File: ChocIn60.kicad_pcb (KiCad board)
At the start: 2 copper layers, 100 x 65 mm, 31 parts, among them J1 USB_B_Micro, J2 AVR-ISP-6, J3 Conn_01x30, J4 Conn_01x04, SW1 SW_Push, U1 ATmega32U4-AU, Y1 16MHz

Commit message: 差動ペア配線
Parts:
- D2: footprint Package_TO_SOT_SMD:SOT-143 -> Orbit_locallib:SOT143B
- moved U1 88.7 mm to (88.1, 78.0), turned to 270 degrees
- moved D2 82.8 mm to (57.7, 58.2), turned to 270 degrees
- moved R2 74.8 mm to (56.3, 65.0), turned to 90 degrees
- moved R1 73.0 mm to (59.1, 65.0), turned to 90 degrees
- moved J1 71.3 mm to (58.0, 52.6)
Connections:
- net Net-(D2-Pad2) renamed /D_P
- net Net-(D2-Pad3) renamed /D_N
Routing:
- net D+: track 0.00 -> 34.2 mm
- net D-: track 0.00 -> 34.1 mm
- net /D_P: track 0.00 -> 10.9 mm
- net /D_N: track 0.00 -> 10.9 mm
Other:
- net class V added: clearance 0.2, trace_width 0.4, via_dia 0.8, via_drill 0.4

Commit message: [WIP] 電源周り
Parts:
- moved D1 91.2 mm to (49.5, 83.8), turned to 90 degrees
- moved F1 82.9 mm to (49.5, 75.8), turned to 90 degrees
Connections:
- U1 pad 14: GND -> +5V
- U1 pad 24: GND -> +5V
- U1 pad 34: GND -> +5V
- U1 pad 44: GND -> +5V
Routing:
- net VCC: track 0.00 -> 23.2 mm
- net VBUS: track 0.00 -> 4.90 mm
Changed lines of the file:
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@@
     (thickness 1.6)
     (drawings 229)
-    (tracks 30)
+    (tracks 34)
     (zones 0)
     (modules 31)
@@
     (solder_mask_min_width 0.25)
     (aux_axis_origin 0 0)
-    (visible_elements 7FFFF7FF)
+    (visible_elements 7FFFFFFF)
     (pcbplotparams
       (layerselection 0x010fc_ffffffff)
@@
     )
     (pad 44 smd rect (at -4 5.7 180) (size 1.5 0.55) (layers B.Cu B.Paste B.Mask)
-      (net 1 GND))
+      (net 5 +5V))
     (pad 43 smd rect (at -3.2 5.7 180) (size 1.5 0.55) (layers B.Cu B.Paste B.Mask)
       (net 1 GND))
@@
       (net 1 GND))
     (pad 34 smd rect (at 4 5.7 180) (size 1.5 0.55) (layers B.Cu B.Paste B.Mask)
-      (net 1 GND))
+      (net 5 +5V))
     (pad 33 smd rect (at 5.7 4 270) (size 1.5 0.55) (layers B.Cu B.Paste B.Mask)
       (net 37 "Net-(R5-Pad2)"))
@@
       (net 23 PD4))
     (pad 24 smd rect (at 5.7 -3.2 270) (size 1.5 0.55) (layers B.Cu B.Paste B.Mask)
-      (net 1 GND))
+      (net 5 +5V))
     (pad 23 smd rect (at 5.7 -4 270) (size 1.5 0.55) (layers B.Cu B.Paste B.Mask)
       (net 1 GND))
@@
       (net 1 GND))
     (pad 14 smd rect (at -2.4 -5.7 180) (size 1.5 0.55) (layers B.Cu B.Paste B.Mask)
-      (net 1 GND))
+      (net 5 +5V))
     (pad 13 smd rect (at -3.2 -5.7 180) (size 1.5 0.55) (layers B.Cu B.Paste B.Mask)
       (net 9 ~RESET))
@@
   )
   (module Fuse:Fuse_1206_3216Metric_Pad1.42x1.75mm_HandSolder (layer B.Cu)
-    (at -9.602 17.749)
+    (at 49.53 75.7825 90)
     (descr "Fuse SMD 1206 (3216 Metric), square (rectangular) end terminal, IPC_7351 nominal with elongated pad for handsoldering. (Body size source: http://www.tortai-tech.com/upload/download/2011102023233369053.pdf), generated with kicad-footprint-generator")
     (tags "resistor handsolder")
     (attr smd)
-    (fp_text reference F1 (at 0 1.82) (layer B.SilkS)
-      (effects (font (size 1 1) (thickness 0.15)) (justify mirror))
-    )
-    (fp_text value 500mA (at 0 -1.82) (layer B.Fab)
-      (effects (font (size 1 1) (thickness 0.15)) (justify mirror))
-    )
-    (fp_text user %R (at 0 0) (layer B.Fab)
+    (fp_text reference F1 (at 0 1.82 90) (layer B.SilkS)
+      (effects (font (size 1 1) (thickness 0.15)) (justify mirror))
+    )
+    (fp_text value 500mA (at 0 -1.82 90) (layer B.Fab)
+      (effects (font (size 1 1) (thickness 0.15)) (justify mirror))
+    )
+    (fp_text user %R (at 0 0 90) (layer B.Fab)
       (effects (font (size 0.8 0.8) (thickness 0.12)) (justify mirror))
     )
@@
     (fp_line (start -1.6 0.8) (end 1.6 0.8) (layer B.Fab) (width 0.1))
     (fp_line (start -1.6 -0.8) (end -1.6 0.8) (layer B.Fab) (width 0.1))
-    (pad 2 smd roundrect (at 1.4875 0) (size 1.425 1.75) (layers B.Cu B.Paste B.Mask) (roundrect_rratio 0.175439)
+    (pad 2 smd roundrect (at 1.4875 0 90) (size 1.425 1.75) (layers B.Cu B.Paste B.Mask) (roundrect_rratio 0.175439)
       (net 7 VCC))
-    (pad 1 smd roundrect (at -1.4875 0) (size 1.425 1.75) (layers B.Cu B.Paste B.Mask) (roundrect_rratio 0.175439)
+    (pad 1 smd roundrect (at -1.4875 0 90) (size 1.425 1.75) (layers B.Cu B.Paste B.Mask) (roundrect_rratio 0.175439)
       (net 6 VBUS))
     (model ${KISYS3DMOD}/Fuse.3dshapes/Fuse_1206_3216Metric.wrl
@@
   )
   (module Diode_SMD:D_SOD-123 (layer B.Cu)
-    (at -9.702 14.429)
+    (at 49.53 83.82 90)
     (descr SOD-123)
     (tags SOD-123)
     (attr smd)
-    (fp_text reference D1 (at 0 2) (layer B.SilkS)
-      (effects (font (size 1 1) (thickness 0.15)) (justify mirror))
-    )
-    (fp_text value Schottky (at 0 -2.1) (layer B.Fab)
+    (fp_text reference D1 (at 0 2 90) (layer B.SilkS)
+      (effects (font (size 1 1) (thickness 0.15)) (justify mirror))
+    )
+    (fp_text value Schottky (at 0 -2.1 90) (layer B.Fab)
       (effects (font (size 1 1) (thickness 0.15)) (justify mirror))
     )
@@
     (fp_line (start 0.25 0) (end 0.75 0) (layer B.Fab) (width 0.1))
     (fp_line (start -2.25 1) (end -2.25 -1) (layer B.SilkS) (width 0.12))
-    (fp_text user %R (at 0 2) (layer B.Fab)
-      (effects (font (size 1 1) (thickness 0.15)) (justify mirror))
-    )
-    (pad 2 smd rect (at 1.65 0) (size 0.9 1.2) (layers B.Cu B.Paste B.Mask)
+    (fp_text user %R (at 0 2 90) (layer B.Fab)
+      (effects (font (size 1 1) (thickness 0.15)) (justify mirror))
+    )
+    (pad 2 smd rect (at 1.65 0 90) (size 0.9 1.2) (layers B.Cu B.Paste B.Mask)
       (net 6 VBUS))
-    (pad 1 smd rect (at -1.65 0) (size 0.9 1.2) (layers B.Cu B.Paste B.Mask)
+    (pad 1 smd rect (at -1.65 0 90) (size 0.9 1.2) (layers B.Cu B.Paste B.Mask)
       (net 5 +5V))
     (model ${KISYS3DMOD}/Diode_SMD.3dshapes/D_SOD-123.wrl
@@
   (gr_line (start 30 86.2) (end 334 86.2) (angle 90) (layer Eco1.User) (width 0.381))
   (gr_line (start 334 107.5) (end 30 107.5) (angle 90) (layer Eco1.User) (width 0.381))
+  (segment (start 49.53 77.27) (end 49.53 82.17) (width 0.4) (layer B.Cu) (net 6))
+  (segment (start 56.7 54.55) (end 56.7 54.05) (width 0.4) (layer B.Cu) (net 7))
+  (segment (start 49.53 61.72) (end 56.7 54.55) (width 0.4) (layer B.Cu) (net 7))
+  (segment (start 49.53 74.295) (end 49.53 61.72) (width 0.4) (layer B.Cu) (net 7))
   (segment (start 57.785 66.421) (end 58.42 65.786) (width 0.2) (layer B.Cu) (net 35))
   (segment (start 57.785 66.929) (end 57.785 66.421) (width 0.2) (layer B.Cu) (net 35))

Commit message: [WIP] 仮配置・仮配線
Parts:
- moved J3 143.3 mm to (110.0, 110.0), turned to 90 degrees
- moved R7 127.7 mm to (111.5, 63.5)
- moved C6 125.2 mm to (90.4, 89.3)
- moved C2 119.6 mm to (98.7, 74.9), turned to 270 degrees
- moved C5 119.3 mm to (79.4, 82.9), turned to 90 degrees
- moved Y1 117.5 mm to (102.6, 77.5), turned to 90 degrees
- moved C3 113.9 mm to (87.2, 65.5), turned to 180 degrees
- moved J2 111.7 mm to (99.0, 63.0), turned to 90 degrees
- moved C4 105.0 mm to (98.6, 70.5), turned to 180 degrees
- moved C1 103.6 mm to (98.7, 78.7), turned to 270 degrees
- moved R5 103.6 mm to (84.1, 90.3), turned to 90 degrees
- moved SW1 99.5 mm to (69.2, 98.2)
- moved C7 99.1 mm to (79.4, 73.2), turned to 90 degrees
- moved J4 95.2 mm to (113.0, 60.5), turned to 90 degrees
- moved R6 93.6 mm to (106.9, 63.5)
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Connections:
- net Net-(C3-Pad1) renamed /UCAP
- C2 pad 1: Net-(C2-Pad1) -> GND
- C2 pad 2: GND -> Net-(C2-Pad2)
- J4 pad 1: +5V -> GND
- J4 pad 2: PD0_SCL -> PD1_SDA
- J4 pad 3: PD1_SDA -> PD0_SCL
- J4 pad 4: GND -> +5V
- R7 pad 1: +5V -> PD1_SDA
- R7 pad 2: PD1_SDA -> +5V
- SW1 pad 1: GND -> ~RESET
- SW1 pad 2: ~RESET -> GND
- SW1 pad 3: GND -> ~RESET
- SW1 pad 4: ~RESET -> GND
- U1 pad 16: Net-(C2-Pad1) -> Net-(C2-Pad2)
- Y1 pad 3: Net-(C2-Pad1) -> Net-(C2-Pad2)
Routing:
- net +5V: track 0.00 -> 117.8 mm, vias 0 -> 6
- net GND: track 0.00 -> 48.6 mm, vias 0 -> 2
- net VBUS: track 4.90 -> 51.7 mm, vias 0 -> 2
- net PD1_SDA: track 0.00 -> 39.7 mm
- net PD0_SCL: track 0.00 -> 38.1 mm
- net PB2_MOSI: track 0.00 -> 14.9 mm
- net ~RESET: track 0.00 -> 13.4 mm, vias 0 -> 1
- net PB3_MISO: track 0.00 -> 12.1 mm
- net Net-(C2-Pad2): track 0.00 -> 11.9 mm
- net PB1_SCK: track 0.00 -> 11.7 mm
- net Net-(C1-Pad1): track 0.00 -> 7.84 mm
- net /UCAP: track 0.00 -> 6.75 mm
- net PB7: track 0.00 -> 4.36 mm, vias 0 -> 1
- net PD2: track 0.00 -> 3.42 mm
- net PD3: track 0.00 -> 2.43 mm
- added copper zone on B.Cu, net GND
- added copper zone on F.Cu, net GND

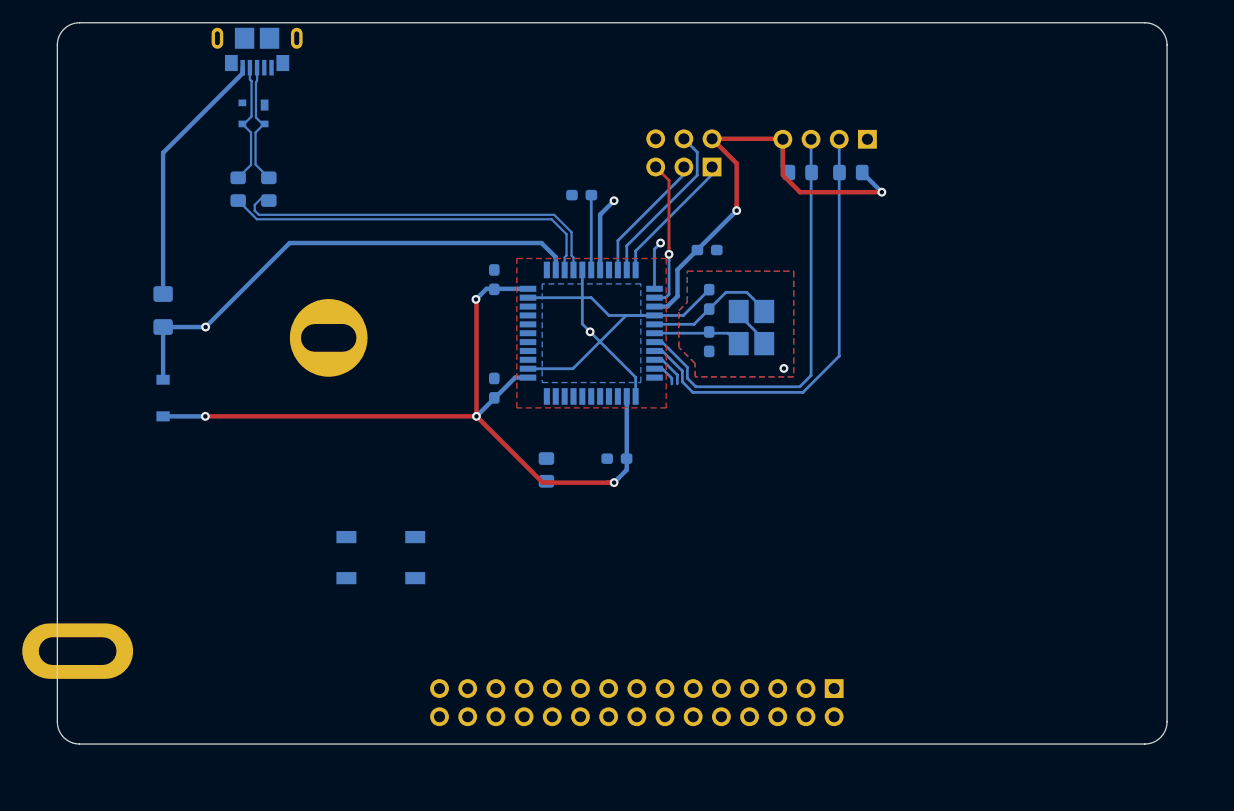
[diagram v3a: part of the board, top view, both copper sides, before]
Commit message: USB-C 復活
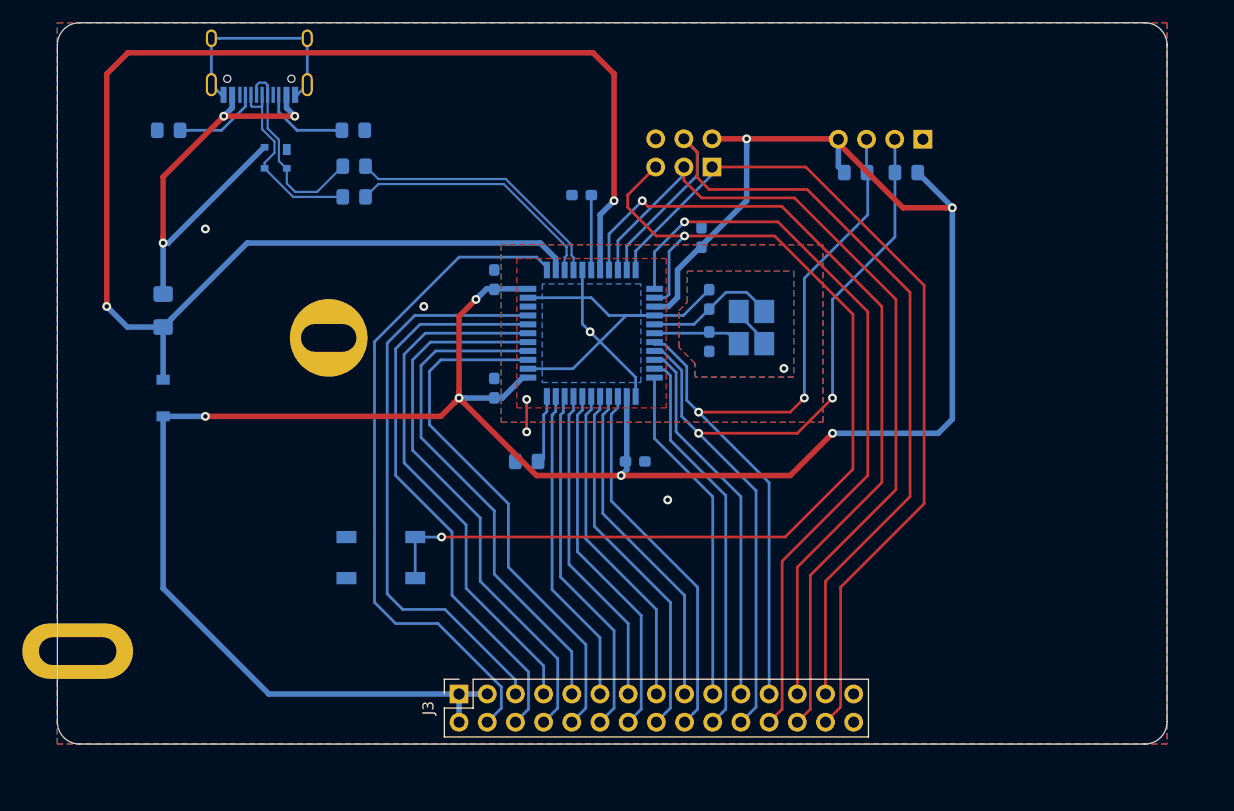
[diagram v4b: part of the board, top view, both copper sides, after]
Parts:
- removed J1: USB_B_Micro, Connector_USB:USB_Micro-B_GCT_USB3076-30-A
- added R3: 5.1k, Resistor_SMD:R_0805_2012Metric_Pad1.15x1.40mm_HandSolder, B.Cu at (66.7, 59.7)
- added R4: 5.1k, Resistor_SMD:R_0805_2012Metric_Pad1.15x1.40mm_HandSolder, B.Cu at (50.0, 59.7)
- added USB1: HRO-TYPE-C-31-M-12, Orbit_Type-C:HRO-TYPE-C-31-M-12, B.Cu at (58.2, 48.8)
- J3: moved to F.Cu
- moved J3 33.8 mm to (76.2, 110.5)
- moved R2 10.5 mm to (66.7, 65.7), turned to 180 degrees
- moved R1 7.96 mm to (66.7, 62.9), turned to 180 degrees
- moved J4 5.00 mm to (118.0, 60.5)
- moved R6 5.00 mm to (111.9, 63.5)
- moved R7 5.00 mm to (116.5, 63.5)
- moved D2 4.47 mm to (59.7, 62.2)
- moved R5 1.93 mm to (82.3, 89.5), turned to 0 degrees
- moved C6 1.67 mm to (92.1, 89.5)
- moved C4 1.24 mm to (98.0, 69.4), turned to 270 degrees
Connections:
- C6 pad 1: GND -> +5V
- C6 pad 2: +5V -> GND
- J3 pad 10: PB6 -> PF7
- J3 pad 11: PB7 -> PC7
- J3 pad 13: PC7 -> PB6
- J3 pad 14: PD0_SCL -> PB5
- J3 pad 15: PD1_SDA -> PB4
- J3 pad 16: PD2 -> PD7
- J3 pad 17: PD3 -> PD6
- J3 pad 20: PD6 -> PD3
- J3 pad 21: PD7 -> PD2
- J3 pad 22: PE6 -> PD1_SDA
- J3 pad 23: PF0 -> PD0_SCL
- J3 pad 24: PF1 -> PB7
- J3 pad 25: PF4 -> PB0
- J3 pad 26: PF5 -> PB1_SCK
- J3 pad 27: PF6 -> PB2_MOSI
- J3 pad 28: PF7 -> PB3_MISO
- J3 pad 4: PB0 -> PE6
- J3 pad 5: PB1_SCK -> PF0
- J3 pad 6: PB2_MOSI -> PF1
- J3 pad 7: PB3_MISO -> PF4
- J3 pad 8: PB4 -> PF5
- J3 pad 9: PB5 -> PF6
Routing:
- net +5V: track 117.8 -> 227.2 mm, vias 6 -> 7
- net VBUS: track 51.7 -> 137.2 mm
- net ~RESET: track 13.4 -> 95.9 mm, vias 1 -> 2
- net PB0: track 0.00 -> 71.1 mm, vias 0 -> 1
- net PB2_MOSI: track 14.9 -> 81.7 mm
- net PB3_MISO: track 12.1 -> 78.7 mm
- net PB1_SCK: track 11.7 -> 78.3 mm
- net PB7: track 4.36 -> 67.7 mm
- net PE6: track 0.00 -> 61.1 mm
- net PF0: track 0.00 -> 52.4 mm
- net PF1: track 0.00 -> 51.9 mm
- net PF5: track 0.00 -> 49.7 mm
- net PF4: track 0.00 -> 47.8 mm
- net PF7: track 0.00 -> 47.3 mm
- net PF6: track 0.00 -> 45.4 mm
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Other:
- net class D added: clearance 0.2, trace_width 0.2, via_dia 0.8, via_drill 0.4
- net class V: trace_width 0.4 -> 0.5

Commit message: ひとまず一通りやり切った……？
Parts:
- removed S2, S3: Screw, gh60_hole:PKRH
- removed S5: Screw, gh60_hole:PKRHSL
- removed S6, S7, S8, S9: Screw_Tofu, gh60_hole:PKRH
- moved C3 1.26 mm to (88.1, 64.6), turned to 90 degrees
- moved R3 0.63 mm to (66.7, 59.1)
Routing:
- net D-: track 23.1 -> 24.6 mm
- net D+: track 23.8 -> 24.7 mm
- net GND: vias 7 -> 45
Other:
- board text removed: "+"
- board text removed: "-"
- board text removed: "0"
- board text removed: "1"
- board text removed: "2"
- board text removed: "3"
- board text removed: "Fn"
- board text removed: "GPIO"
- board text removed: "PCB design by komar007 & jdcarpe"
- board text removed: "Poker arrows"
- board text removed: "R1"
- board text removed: "R2"
- board text removed: "R3"
- board text removed: "R4"
- board text removed: "R5"
- board text removed: "dedicated to the memory of SmallFry"
- board text removed: "expansion module"
- board text removed: "http://gh60.info"
